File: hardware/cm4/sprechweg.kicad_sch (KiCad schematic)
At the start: 9 parts, among them J2 D340 Audio, T1 600:600, T2 600:600

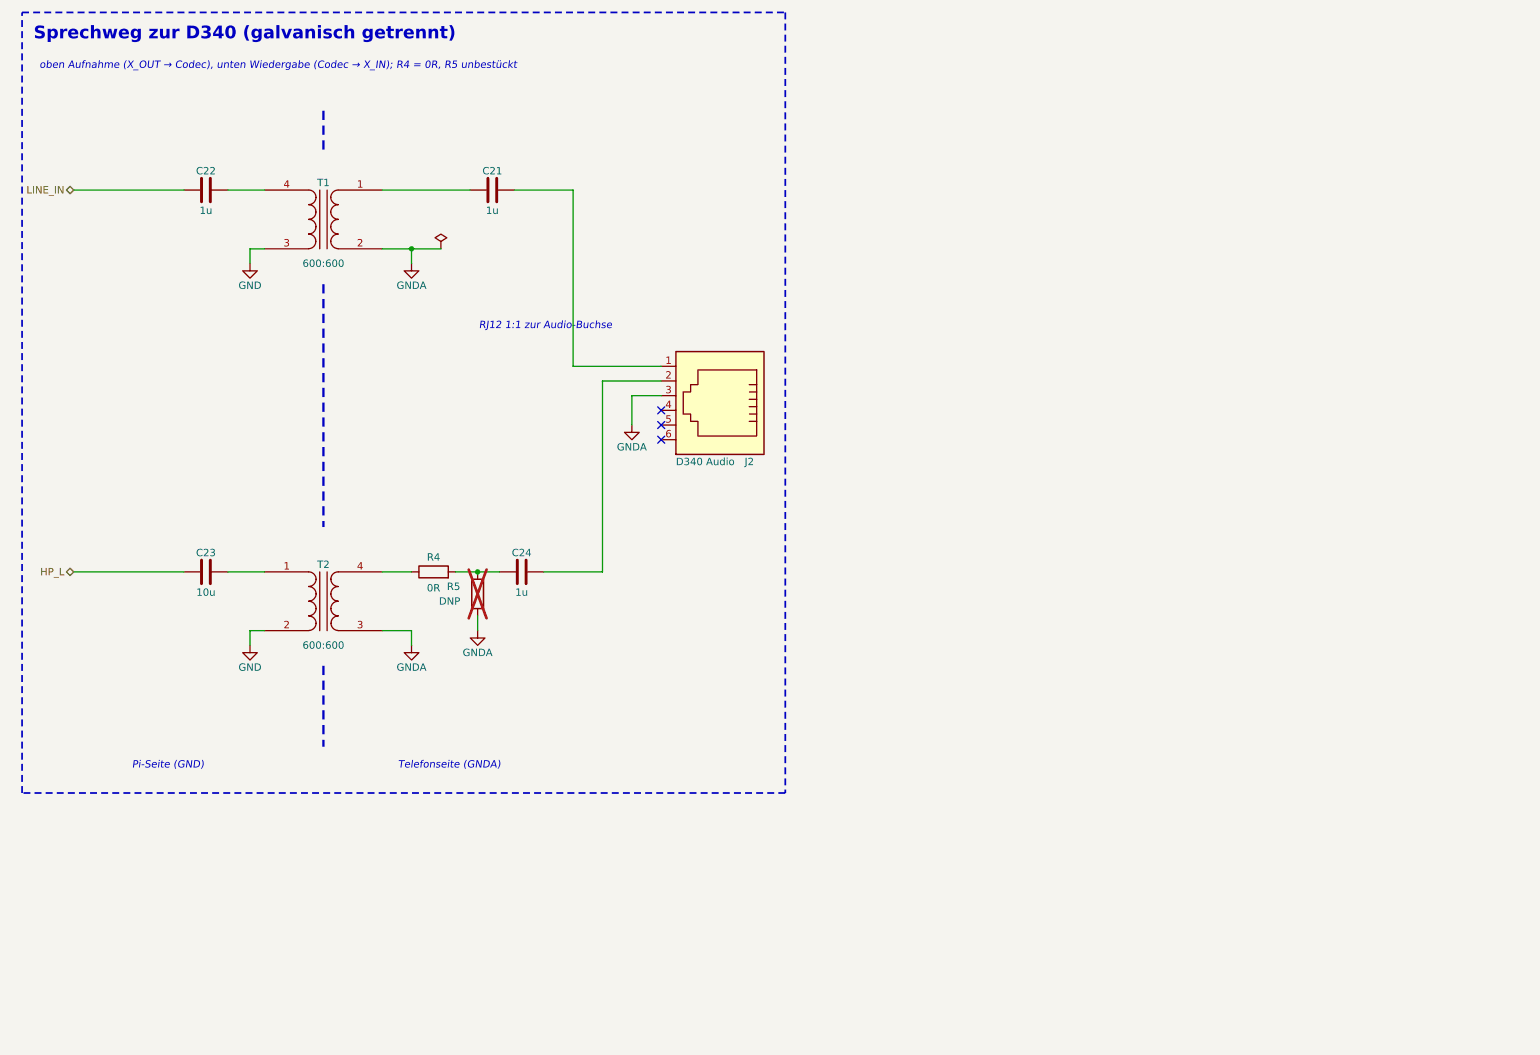
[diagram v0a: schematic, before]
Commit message: CM4-Schaltplan: Einzelblock-Blätter ohne Rahmen, Inhalt zentriert
kicadgen: Steht nur ein Block auf einem Blatt, entfällt der Rahmen (sein Titel wird
Blatttitel) und der Inhalt wird auf dem Blatt zentriert (über dem Schriftfeld, auf dem
1,27-mm-Raster). Hinweistexte der CM4-Blätter an die Schaltungen gerückt.

Co-Authored-By: Claude Opus 5.5 <noreply@anthropic.com>
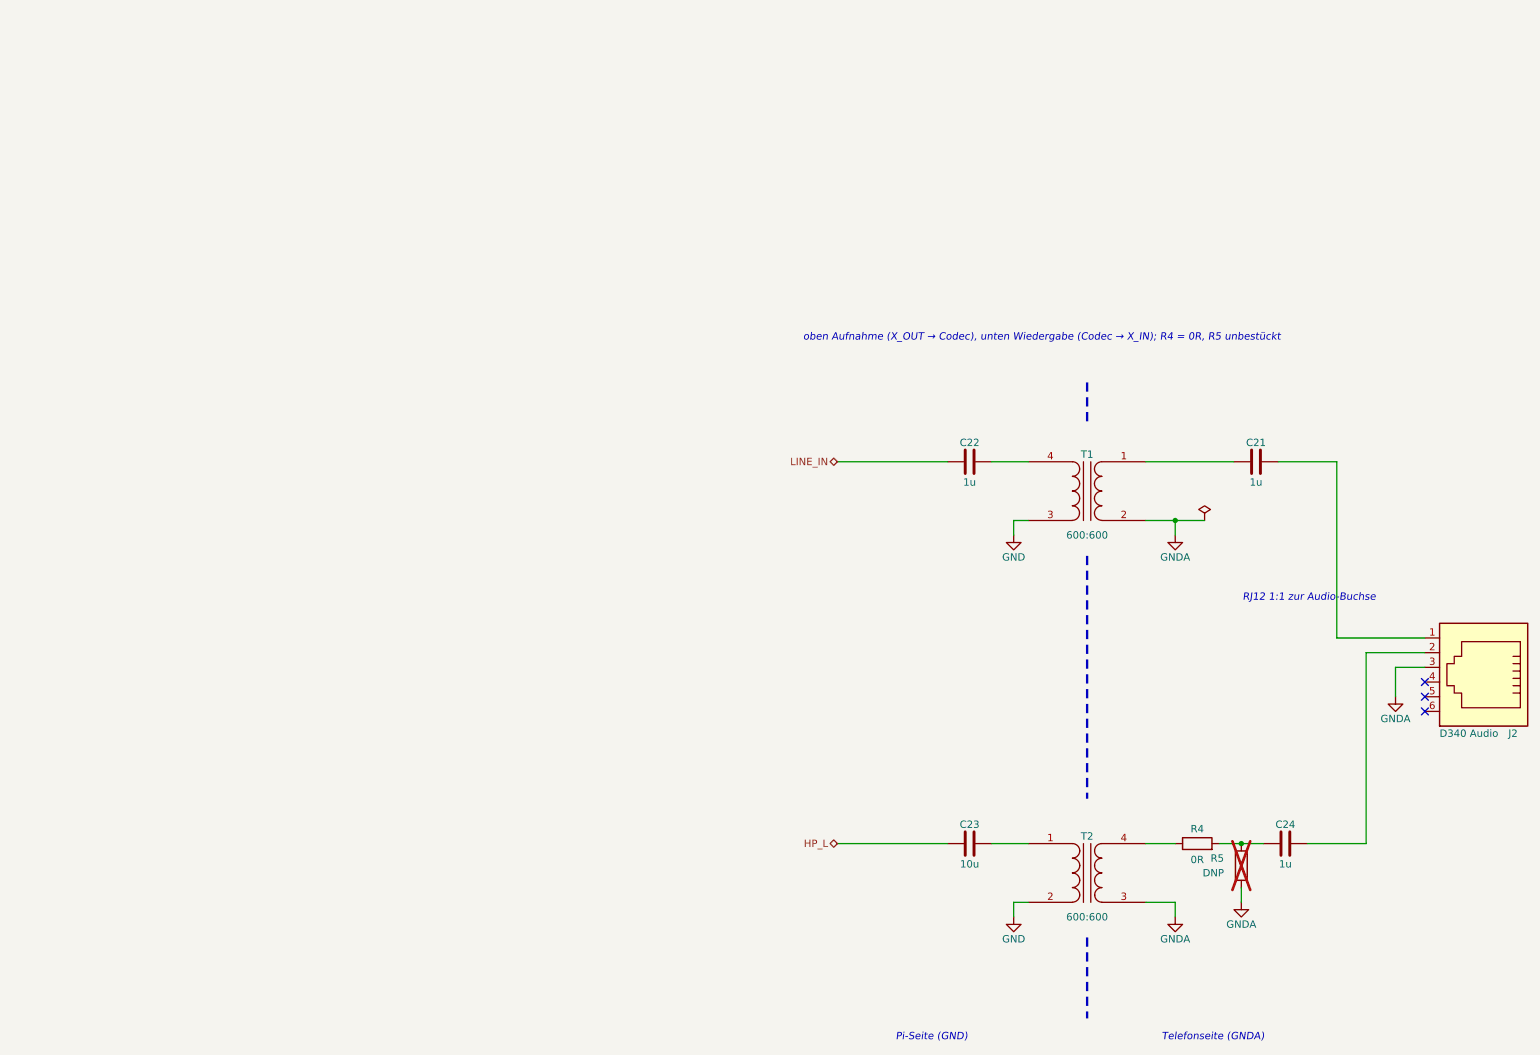
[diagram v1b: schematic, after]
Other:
- note removed: "Sprechweg zur D340 (galvanisch getrennt)"
- title: Sprechweg -> Sprechweg zur D340 (galvanisch getrennt)
